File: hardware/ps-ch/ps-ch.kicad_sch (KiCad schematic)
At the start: 72 parts, among them Q11 BSS138, U10 ADuM1401xRW, U11 LMR51610X, U13 ADuM1401xRW, U3 LM61495, U5 OPA992IDBVR

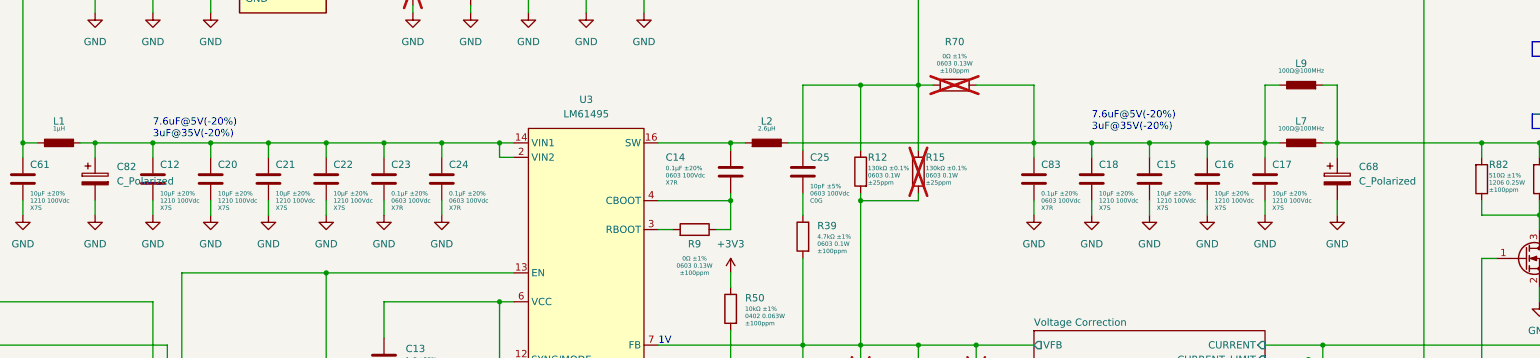
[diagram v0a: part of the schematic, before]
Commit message: assigned footprints
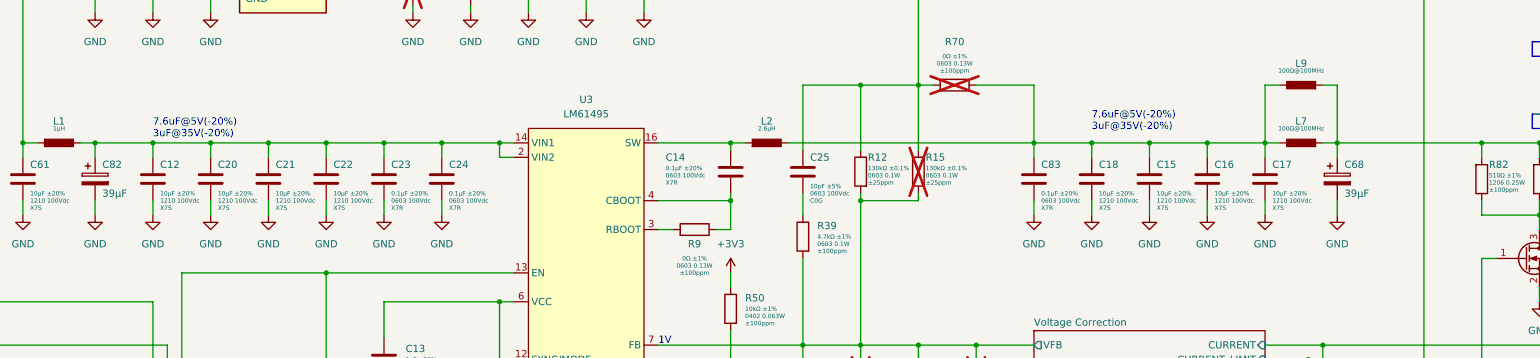
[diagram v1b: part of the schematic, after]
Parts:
- C68, C82: value C_Polarized -> 39µF; footprint (none) -> Capacitor_SMD:CP_Elec_8x11.9; symbol Device:C_Polarized -> ps-ch:875075855005; Manufacturer (none) -> Wuerth Elektronik; Manufacturer Part Number (none) -> 875075855005
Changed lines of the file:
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@@
 	)
 	(symbol
-		(lib_id "Device:C_Polarized")
+		(lib_id "ps-ch:875075855005")
 		(at 403.86 95.25 0)
 		(unit 1)
@@
 		(on_board yes)
 		(dnp no)
-		(fields_autoplaced yes)
 		(property "Reference" "C68"
-			(at 407.67 93.0909 0)
+			(at 405.13 92.71 0)
 			(effects
 				(font
@@
 			)
 		)
-		(property "Value" "C_Polarized"
-			(at 407.67 95.6309 0)
+		(property "Value" "39µF"
+			(at 405.13 97.79 0)
 			(effects
 				(font
@@
 			)
 		)
-		(property "Footprint" ""
-			(at 404.8252 99.06 0)
+		(property "Footprint" "Capacitor_SMD:CP_Elec_8x11.9"
+			(at 403.86 82.55 0)
 			(effects
 				(font
@@
 			)
 		)
-		(property "Datasheet" "~"
-			(at 403.86 95.25 0)
+		(property "Datasheet" "https://www.we-online.com/components/products/datasheet/875075855005.pdf"
+			(at 403.86 80.01 0)
 			(effects
 				(font
@@
 		)
 		(property "Description" "Polarized capacitor"
-			(at 403.86 95.25 0)
+			(at 403.86 77.47 0)
+			(effects
+				(font
+					(size 1.27 1.27)
+				)
+				(hide yes)
+			)
+		)
+		(property "Manufacturer" "Wuerth Elektronik"
+			(at 403.86 72.39 0)
+			(effects
+				(font
+					(size 1.27 1.27)
+				)
+				(hide yes)
+			)
+		)
+		(property "Manufacturer Part Number" "875075855005"
+			(at 403.86 74.93 0)
 			(effects
 				(font
@@
 	)
 	(symbol
-		(lib_id "Device:C_Polarized")
+		(lib_id "ps-ch:875075855005")
 		(at 185.42 95.25 0)
 		(unit 1)
@@
 		(on_board yes)
 		(dnp no)
-		(fields_autoplaced yes)
 		(property "Reference" "C82"
-			(at 189.23 93.0909 0)
+			(at 186.69 92.71 0)
 			(effects
 				(font
@@
 			)
 		)
-		(property "Value" "C_Polarized"
-			(at 189.23 95.6309 0)
+		(property "Value" "39µF"
+			(at 186.69 97.79 0)
 			(effects
 				(font
@@
 			)
 		)
-		(property "Footprint" ""
-			(at 186.3852 99.06 0)
+		(property "Footprint" "Capacitor_SMD:CP_Elec_8x11.9"
+			(at 185.42 82.55 0)
 			(effects
 				(font
@@
 			)
 		)
-		(property "Datasheet" "~"
-			(at 185.42 95.25 0)
+		(property "Datasheet" "https://www.we-online.com/components/products/datasheet/875075855005.pdf"
+			(at 185.42 80.01 0)
 			(effects
 				(font
@@
 		)
 		(property "Description" "Polarized capacitor"
-			(at 185.42 95.25 0)
+			(at 185.42 77.47 0)
+			(effects
+				(font
+					(size 1.27 1.27)
+				)
+				(hide yes)
+			)
+		)
+		(property "Manufacturer" "Wuerth Elektronik"
+			(at 185.42 72.39 0)
+			(effects
+				(font
+					(size 1.27 1.27)
+				)
+				(hide yes)
+			)
+		)
+		(property "Manufacturer Part Number" "875075855005"
+			(at 185.42 74.93 0)
 			(effects
 				(font

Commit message: added snubber circuit components
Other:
- note added: "feedback?! better behind switch?!"
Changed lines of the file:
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@@
 		)
 	)
+	(text "feedback?! better behind switch?!"
+		(exclude_from_sim no)
+		(at 528.32 72.39 0)
+		(effects
+			(font
+				(size 1.27 1.27)
+				(color 255 0 0 1)
+			)
+		)
+	)
 	(text "7.6uF@5V(-20%)\n3uF@35V(-20%)"
 		(exclude_from_sim no)
@@
 			(effects
 				(font
-					(size 1.27 1.27)
+					(size 0.762 0.762)
+					(color 132 0 132 1)
 				)
 				(justify left)
@@
 			(effects
 				(font
-					(size 1.27 1.27)
+					(size 0.762 0.762)
+					(color 132 0 132 1)
 				)
 				(justify left)

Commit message: changed voltage sensing circuit
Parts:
- removed R70, R71: 0Ω 0603 0.1W ±1% ±100ppm/°C, Resistor_SMD:R_0603_1608Metric, symbol ps-ch:0Ω 0603 0.1W ±1% ±100ppm/°C
- added C89: 0.1μF 0603 100Vdc X7R ±20%, Capacitor_SMD:C_0603_1608Metric, symbol ps-ch:0.1μF 0603 100Vdc X7R ±20%
- added D7: PMEG60T30ELR, Diode_SMD:Nexperia_CFP3_SOD-123W, symbol ps-ch:PMEG60T30ELR
- added K1: Relay_DPDT, symbol Relay:Relay_DPDT
- added Q12: BSS138, Package_TO_SOT_SMD:SOT-23, symbol Transistor_FET:BSS138
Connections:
- net +3V3: now also C89.2, D7.1 (K), K1.A1
- net Current Measurement/OUT: no longer R69.2
- net GND: now also C89.1, K1.22, Q12.2 (S)
- net Voltage Correction/VSENSE+: now also K1.11
- net Voltage Correction/VSENSE-: now also K1.21
- net at C15.2, C16.2, C17.2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: now also C25.2, R12.1, R15.1
- new net: D7.2 (A), K1.A2, Q12.3 (D)
- new net STM32/EN_EXT_VSENSE: Q12.1 (G)
- new net VOUT: K1.12, R69.2
- new net VSENSE+: K1.14
- new net VSENSE-: K1.24
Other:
- sheet STM32 ports: added EN_EXT_VSENSE; removed ADC0, DISABLE_VOLTAGE_SENSING
- sheet Voltage Correction ports: added none; removed DISABLE_VOLTAGE_SENSING
- note added: "TX2SA-3V"
- note removed: "feedback?! better behind switch?!"

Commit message: created and assigned footprints
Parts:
- removed K1: Relay_DPDT, symbol Relay:Relay_DPDT
- added K1: TX2SA-3V, ps-ch:ATX203SA, symbol ps-ch:TX2SA-3V
- L1: footprint (none) -> ps-ch:WE-HCI_5040
- L2: footprint (none) -> ps-ch:WE-HCI_1890
- L5: footprint (none) -> ps-ch:WE-LQS_6045
- L7, L9: footprint (none) -> ps-ch:WE-MPSB_2220
- U3: footprint (none) -> ps-ch:VQFN-HR(16); Manufacturer (none) -> Texas Instruments; Manufacturer Part Number (none) -> LM61495RPHR
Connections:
- net +3V3: now also K1.1
- net GND: now also K1.10
- net VOUT: now also K1.3
- net VSENSE+: now also K1.5
- net VSENSE-: now also K1.8
- net Voltage Correction/VSENSE+: now also K1.4
- net Voltage Correction/VSENSE-: now also K1.9
- net at D7.2 (A), Q12.3 (D): now also K1.12
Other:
- note removed: "TX2SA-3V"
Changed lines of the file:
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@@
 		)
 	)
-	(text "TX2SA-3V"
-		(exclude_from_sim no)
-		(at 563.88 135.89 0)
-		(effects
-			(font
-				(size 1.27 1.27)
-			)
-		)
-	)
 	(text "7.6uF@5V(-20%)\n3uF@35V(-20%)"
 		(exclude_from_sim no)
@@
 	)
 	(symbol
-		(lib_id "Relay:Relay_DPDT")
-		(at 542.29 132.08 0)
-		(unit 1)
-		(exclude_from_sim no)
-		(in_bom yes)
-		(on_board yes)
-		(dnp no)
-		(fields_autoplaced yes)
-		(property "Reference" "K1"
-			(at 558.8 130.8099 0)
-			(effects
-				(font
-					(size 1.27 1.27)
-				)
-				(justify left)
-			)
-		)
-		(property "Value" "Relay_DPDT"
-			(at 558.8 133.3499 0)
-			(effects
-				(font
-					(size 1.27 1.27)
-				)
-				(justify left)
-			)
-		)
-		(property "Footprint" ""
-			(at 558.8 133.35 0)
-			(effects
-				(font
-					(size 1.27 1.27)
-				)
-				(justify left)
-				(hide yes)
-			)
-		)
-		(property "Datasheet" "~"
-			(at 542.29 132.08 0)
-			(effects
-				(font
-					(size 1.27 1.27)
-				)
-				(hide yes)
-			)
-		)
-		(property "Description" "Relay DPDT, monostable, EN50005"
-			(at 542.29 132.08 0)
-			(effects
-				(font
-					(size 1.27 1.27)
-				)
-				(hide yes)
-			)
-		)
-		(pin "24"
-		)
-		(pin "A2"
-		)
-		(pin "12"
-		)
-		(pin "21"
-		)
-		(pin "14"
-		)
-		(pin "11"
-		)
-		(pin "A1"
-		)
-		(pin "22"
-		)
-		(instances
-			(project ""
-				(path "/431acd2e-2ab9-4aa9-b759-273f044decc5"
-					(reference "K1")
-					(unit 1)
-				)
-			)
-		)
-	)
-	(symbol
 		(lib_id "power:GND")
 		(at 142.24 137.16 0)
@@
 			)
 		)
-		(property "Footprint" ""
+		(property "Footprint" "ps-ch:WE-MPSB_2220"
 			(at 384.81 78.74 0)
 			(effects
@@
 			)
 		)
-		(property "Datasheet" ""
+		(property "Datasheet" "https://www.we-online.com/components/products/datasheet/74279224101.pdf"
 			(at 394.97 78.74 0)
 			(effects
@@
 	)
 	(symbol
+		(lib_id "ps-ch:TX2SA-3V")
+		(at 542.29 132.08 0)
+		(unit 1)
+		(exclude_from_sim no)
+		(in_bom yes)
+		(on_board yes)
+		(dnp no)
+		(fields_autoplaced yes)
+		(property "Reference" "K1"
+			(at 558.8 130.8099 0)
+			(effects
+				(font
+					(size 1.27 1.27)
+				)
+				(justify left)
+			)
+		)
+		(property "Value" "TX2SA-3V"
+			(at 558.8 133.3499 0)
+			(effects
+				(font
+					(size 1.27 1.27)
+				)
+				(justify left)
+			)
+		)
+		(property "Footprint" "ps-ch:ATX203SA"
+			(at 542.29 132.08 0)
+			(effects
+				(font
+					(size 1.27 1.27)
+				)
+				(justify left)
+				(hide yes)
+			)
+		)
+		(property "Datasheet" "~"
+			(at 542.29 132.08 0)
+			(effects
+				(font
+					(size 1.27 1.27)
+				)
+				(hide yes)
+			)
+		)
+		(property "Description" "Relay DPDT, bistable, single-coil, EN50005"
+			(at 542.29 132.08 0)
+			(effects
+				(font
+					(size 1.27 1.27)
+				)
+				(hide yes)
+			)
+		)
+		(property "Manufacturer" "Panasonic"
+			(at 542.29 132.08 0)
+			(effects
+				(font
+					(size 1.27 1.27)
+				)
+				(hide yes)
+			)
+		)
+		(property "Manufacturer Part Number" "TX2SA-3V"
+			(at 542.29 132.08 0)
+			(effects
+				(font
+					(size 1.27 1.27)
+				)
+				(hide yes)
+			)
+		)
+		(pin "8"
+		)
+		(pin "1"
+		)
+		(pin "12"
+		)
+		(pin "3"
+		)
+		(pin "9"
+		)
+		(pin "5"
+		)
+		(pin "4"
+		)
+		(pin "10"
+		)
+		(instances
+			(project ""
+				(path "/431acd2e-2ab9-4aa9-b759-273f044decc5"
+					(reference "K1")
+					(unit 1)
+				)
+			)
+		)
+	)
+	(symbol
 		(lib_id "ps-ch:74279224101")
 		(at 397.51 88.9 90)
@@
 			)
 		)
-		(property "Footprint" ""
+		(property "Footprint" "ps-ch:WE-MPSB_2220"
 			(at 384.81 88.9 0)
 			(effects
@@
 			)
 		)
-		(property "Datasheet" ""
+		(property "Datasheet" "https://www.we-online.com/components/products/datasheet/74279224101.pdf"
 			(at 394.97 88.9 0)
 			(effects
@@
 			)
 		)
-		(property "Footprint" ""
+		(property "Footprint" "ps-ch:WE-HCI_5040"
 			(at 166.37 88.9 0)
 			(effects
@@
 			)
 		)
-		(property "Footprint" ""
+		(property "Footprint" "ps-ch:WE-HCI_1890"
 			(at 290.83 88.9 0)
 			(effects
@@
 			)
 		)
-		(property "Footprint" ""
+		(property "Footprint" "ps-ch:WE-LQS_6045"
 			(at 223.52 43.18 0)
 			(effects
@@
 			)
 		)
-		(property "Footprint" ""
+		(property "Footprint" "ps-ch:VQFN-HR(16)"
 			(at 271.78 119.38 0)
 			(effects
@@
 			(at 271.78 119.38 0)
 			(effects
+				(font
+					(size 1.27 1.27)
+				)
+				(hide yes)
+			)
+		)
+		(property "Manufacturer" "Texas Instruments"
+			(at 271.78 119.38 0)
+			(effects
+				(font
+					(size 1.27 1.27)
+				)
+				(hide yes)
+			)
+		)
+		(property "Manufacturer Part Number" "LM61495RPHR"
+			(at 271.78 119.38 0)
+			(effects

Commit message: first pcb sync
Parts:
- added J1, J2: Conn_02x16_Odd_Even, Connector_PinHeader_2.54mm:PinHeader_2x16_P2.54mm_Vertical, symbol Connector_Generic:Conn_02x16_Odd_Even
- renumbered C48 to C1, C61 to C10, C82 to C11, C20 to C13, C21 to C14, C22 to C15, C23 to C16, C24 to C17, C83 to C18, C18 to C19, C49 to C2, C15 to C20, C16 to C21, C17 to C22, C68 to C23, C13 to C24, C47 to C25, C46 to C26, C19 to C27, C89 to C28, C56 to C29, C51 to C3, C57 to C30, C41 to C31, C33 to C32, C34 to C33, C50 to C4, C52 to C5, C53 to C6, C81 to C7, C14 to C8, C25 to C9, D7 to D1, L6 to L1, L5 to L2, L9 to L3, L1 to L4, L2 to L5, L7 to L6, L4 to L7, Q11 to Q1, Q12 to Q2, R46 to R1, R9 to R10, R39 to R11, R50 to R12, R67 to R13, R13 to R14, R16 to R15, R14 to R16, R62 to R17, R61 to R18, R8 to R19, R69 to R2, R6 to R20, R56 to R21, R58 to R22, R57 to R23, R63 to R24, R81 to R25, R7 to R3, R47 to R4, R54 to R5, R12 to R6, R15 to R7, R82 to R8, R75 to R9, U11 to U1, U3 to U2, U10 to U3, U13 to U4
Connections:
- net 3V3: now also J1.12 (Pin_12), J1.9 (Pin_9), J2.12 (Pin_12), J2.9 (Pin_9)
- net ACTIVATE_BOOTLOADER: now also J1.13 (Pin_13), J2.13 (Pin_13)
- net NRST: now also J1.16 (Pin_16), J2.16 (Pin_16)
- net Earth renamed PRI_LO
- net PRI_LO: now also J1.10 (Pin_10), J1.11 (Pin_11), J1.14 (Pin_14), J1.15 (Pin_15), J1.18 (Pin_18), J1.19 (Pin_19), J1.2 (Pin_2), J1.22 (Pin_22), J1.23 (Pin_23), J1.26 (Pin_26), J1.27 (Pin_27), J1.3 (Pin_3), J1.30 (Pin_30), J1.31 (Pin_31), J1.6 (Pin_6), J1.7 (Pin_7), J2.10 (Pin_10), J2.11 (Pin_11), J2.14 (Pin_14), J2.15 (Pin_15), J2.18 (Pin_18), J2.19 (Pin_19), J2.2 (Pin_2), J2.22 (Pin_22), J2.23 (Pin_23), J2.26 (Pin_26), J2.27 (Pin_27), J2.29 (Pin_29), J2.3 (Pin_3), J2.30 (Pin_30), J2.31 (Pin_31), J2.32 (Pin_32), J2.6 (Pin_6), J2.7 (Pin_7)
- net UART_RX renamed UART0_RX
- net UART0_RX: now also J1.20 (Pin_20)
- net UART_TX renamed UART0_TX
- net UART0_TX: now also J1.17 (Pin_17)
- new net PRI_HI: J1.1 (Pin_1), J1.4 (Pin_4), J1.5 (Pin_5), J1.8 (Pin_8), J2.1 (Pin_1), J2.4 (Pin_4), J2.5 (Pin_5), J2.8 (Pin_8)
- new net UART1_RX: J1.24 (Pin_24), J2.20 (Pin_20)
- new net UART1_TX: J1.21 (Pin_21), J2.17 (Pin_17)
- new net UART2_RX: J1.28 (Pin_28), J2.24 (Pin_24)
- new net UART2_TX: J1.25 (Pin_25), J2.21 (Pin_21)
- new net UART3_RX: J1.32 (Pin_32), J2.28 (Pin_28)
- new net UART3_TX: J1.29 (Pin_29), J2.25 (Pin_25)
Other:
- note added: "INPUT"
- note added: "OUTPUT"

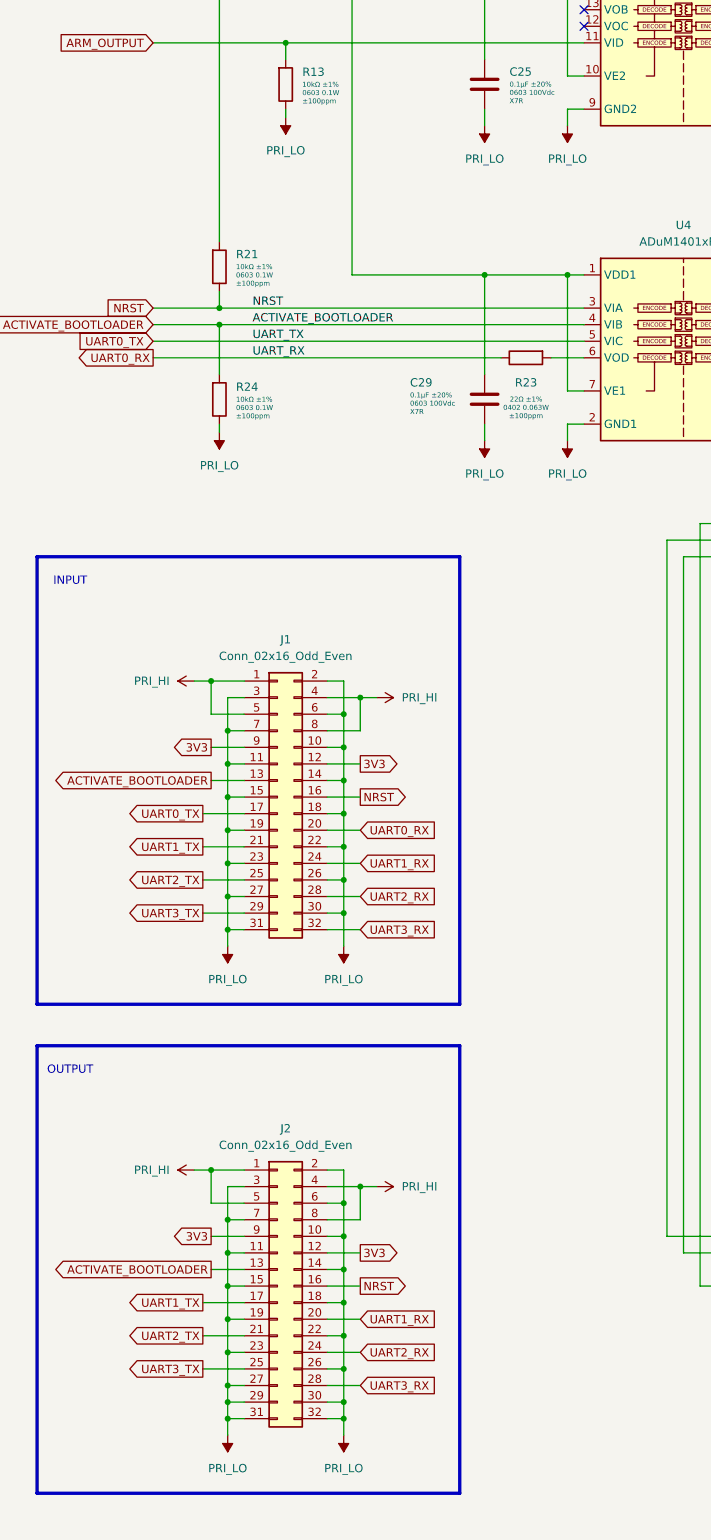
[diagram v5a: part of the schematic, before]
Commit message: removed cmc, replaced input/output connectors
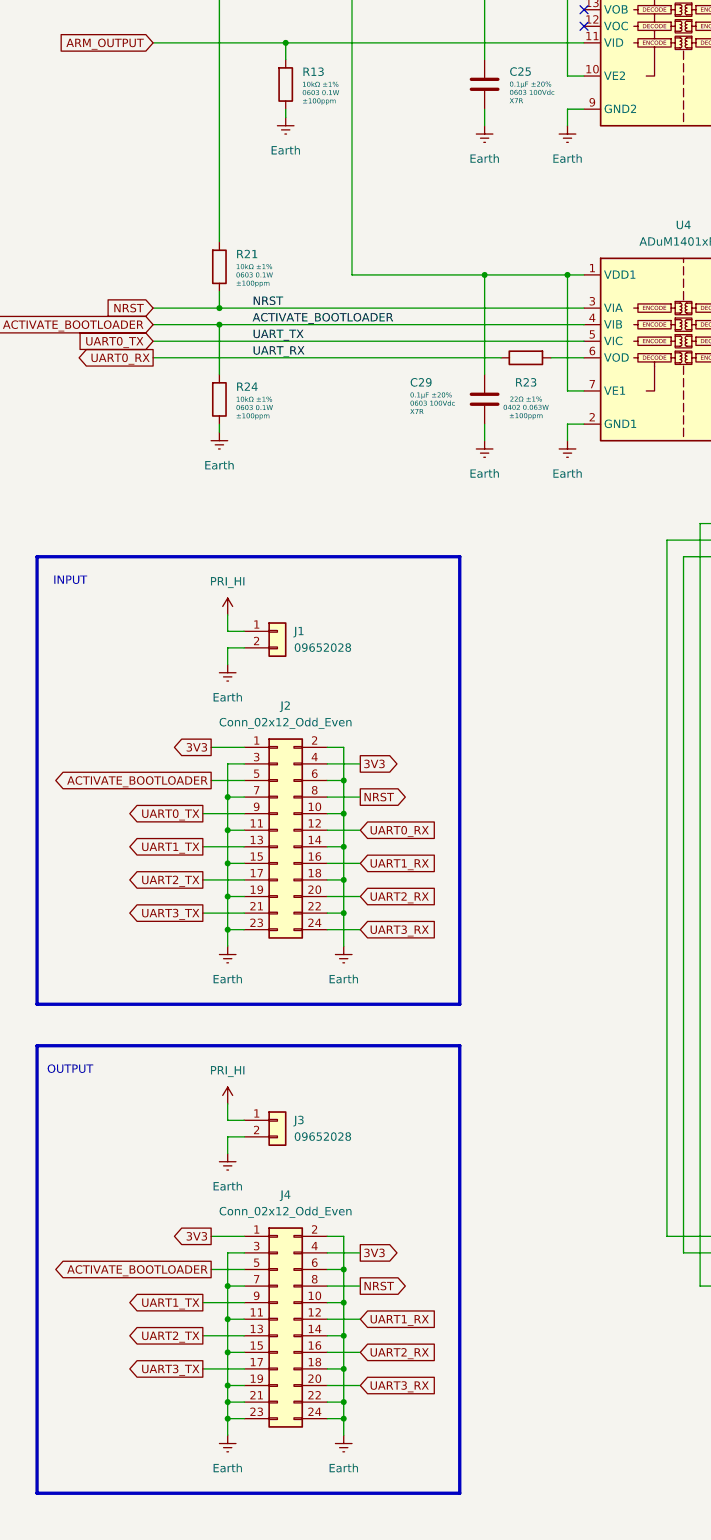
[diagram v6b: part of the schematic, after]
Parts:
- removed J1, J2: Conn_02x16_Odd_Even, Connector_PinHeader_2.54mm:PinHeader_2x16_P2.54mm_Vertical, symbol Connector_Generic:Conn_02x16_Odd_Even
- added J1, J3: 09652028, ps-ch:09652028, symbol ps-ch:09652028
- added J2, J4: Conn_02x12_Odd_Even, Connector_PinHeader_2.54mm:PinHeader_2x12_P2.54mm_Vertical, symbol Connector_Generic:Conn_02x12_Odd_Even
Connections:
- net 3V3: now also J2.1 (Pin_1), J2.4 (Pin_4), J4.1 (Pin_1), J4.4 (Pin_4)
- net ACTIVATE_BOOTLOADER: now also J2.5 (Pin_5), J4.5 (Pin_5)
- net NRST: now also J2.8 (Pin_8), J4.8 (Pin_8)
- net PRI_HI: now also J1.1 (Pin_1), J3.1 (Pin_1)
- net UART0_RX: now also J2.12 (Pin_12)
- net UART0_TX: now also J2.9 (Pin_9)
- net UART1_RX: now also J2.16 (Pin_16), J4.12 (Pin_12)
- net UART1_TX: now also J2.13 (Pin_13), J4.9 (Pin_9)
- net UART2_RX: now also J2.20 (Pin_20), J4.16 (Pin_16)
- net UART2_TX: now also J2.17 (Pin_17), J4.13 (Pin_13)
- net UART3_RX: now also J2.24 (Pin_24), J4.20 (Pin_20)
- net UART3_TX: now also J2.21 (Pin_21), J4.17 (Pin_17)
- net PRI_LO renamed Earth
- net Earth: now also J1.2 (Pin_2), J2.10 (Pin_10), J2.11 (Pin_11), J2.14 (Pin_14), J2.15 (Pin_15), J2.18 (Pin_18), J2.19 (Pin_19), J2.2 (Pin_2), J2.22 (Pin_22), J2.23 (Pin_23), J2.3 (Pin_3), J2.6 (Pin_6), J2.7 (Pin_7), J3.2 (Pin_2), J4.10 (Pin_10), J4.11 (Pin_11), J4.14 (Pin_14), J4.15 (Pin_15), J4.18 (Pin_18), J4.19 (Pin_19), J4.2 (Pin_2), J4.21 (Pin_21), J4.22 (Pin_22), J4.23 (Pin_23), J4.24 (Pin_24), J4.3 (Pin_3), J4.6 (Pin_6), J4.7 (Pin_7)

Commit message: started floorplanning
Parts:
- added H1, H2, H3, H4: MountingHole_Pad, MountingHole:MountingHole_3.2mm_M3_Pad, symbol Mechanical:MountingHole_Pad
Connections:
- net Earth: now also H1.1, H2.1, H3.1, H4.1
- net STM32/DISCHARGE_OUTPUT renamed DISCHARGE
- net STM32/ENABLE_PWR_SPL renamed EN_PWR_SPL
